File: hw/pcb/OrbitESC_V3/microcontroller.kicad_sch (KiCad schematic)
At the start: 57 parts, among them J1 USB_C_Receptacle_USB2.0, J11 CANH, J11 CANL, J11 GND, J13 Micro_SD_Card, SW1 Reset, SW2 DFU, U1 TLE9250X, U2 AT25SF128A-SHB-T, U3 STM32F446RETx, X1 ASE-24MHz

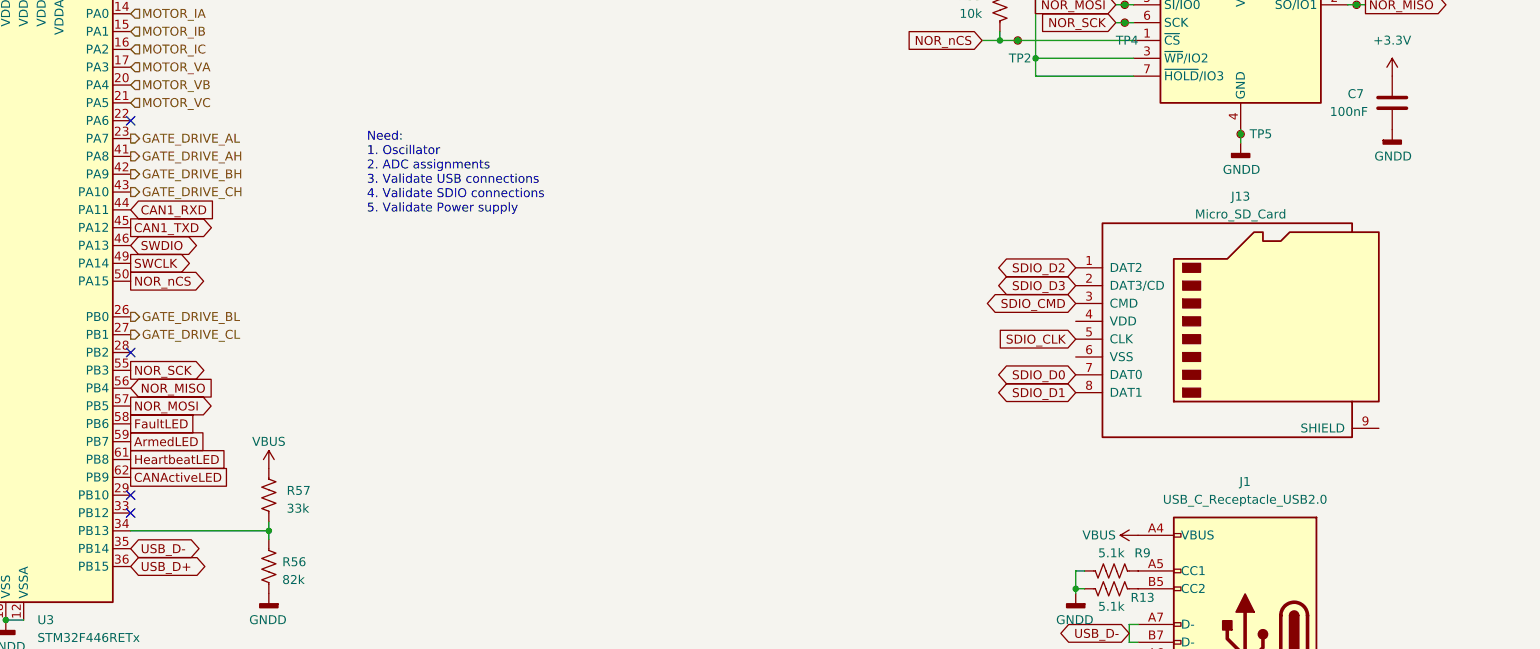
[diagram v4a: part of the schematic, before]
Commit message: Update SDIO card detect
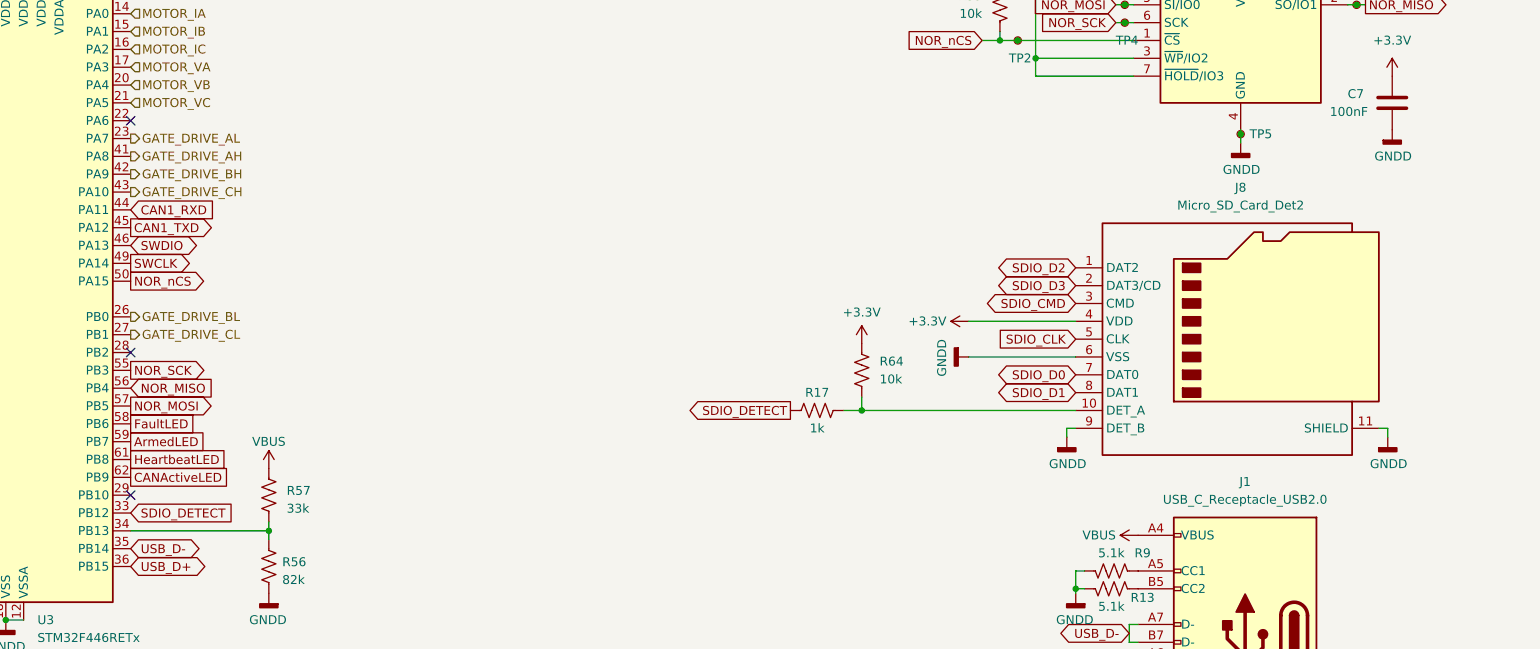
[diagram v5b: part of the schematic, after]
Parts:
- removed J13: Micro_SD_Card, symbol Connector:Micro_SD_Card
- added J8: Micro_SD_Card_Det2, symbol Connector:Micro_SD_Card_Det2
- added R17: 1k, Resistor_SMD:R_0402_1005Metric, symbol Device:R_US
- added R64: 10k, Resistor_SMD:R_0402_1005Metric, symbol Device:R_US
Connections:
- net +3.3V: now also J8.4 (VDD), R64.2
- net GND: now also J8.11 (SHIELD), J8.6 (VSS), J8.9 (DET_B)
- net SDIO_CLK: now also J8.5 (CLK)
- net SDIO_CMD: now also J8.3 (CMD)
- net SDIO_D0: now also J8.7 (DAT0)
- net SDIO_D1: now also J8.8 (DAT1)
- net SDIO_D2: now also J8.1 (DAT2)
- net SDIO_D3: now also J8.2 (DAT3/CD)
- net SDIO_DETECT: now reaches U3.33 (PB12)
- net SDIO_DETECT: now also R17.1
- new net: J8.10 (DET_A), R17.2, R64.1
- no-connect marks 17 -> 16
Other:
- note removed: "Need: 1. Oscillator 2. ADC assignments 3. Validate USB connections 4. Validate SDIO connections 5. Validate Power supply"

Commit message: Sync more work on schematic
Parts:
- C29: LCSC (none) -> C23733
- J8: footprint (none) -> Connector_Card:microSD_HC_Hirose_DM3D-SF; DigiKey (none) -> HR1941CT-ND
- R56: value 82k -> 100k; LCSC (none) -> C25741
- R57: value 33k -> 56k; LCSC (none) -> C25796
- U3: LCSC (none) -> C69336
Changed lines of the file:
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@@
       (effects (font (size 1.27 1.27)) hide)
     )
-    (property "LCSC" "" (at 145.415 205.74 0)
+    (property "LCSC" "C23733" (at 145.415 205.74 0)
       (effects (font (size 1.27 1.27)) hide)
     )
@@
     )
     (property "Datasheet" "https://www.st.com/resource/en/datasheet/stm32f446re.pdf" (at 177.8 175.26 0)
+      (effects (font (size 1.27 1.27)) hide)
+    )
+    (property "LCSC" "C69336" (at 177.8 175.26 0)
       (effects (font (size 1.27 1.27)) hide)
     )
@@
       (effects (font (size 1.27 1.27)) (justify left))
     )
-    (property "Value" "33k" (at 217.805 205.105 0)
+    (property "Value" "56k" (at 217.805 205.105 0)
       (effects (font (size 1.27 1.27)) (justify left))
     )
@@
       (effects (font (size 1.27 1.27)) hide)
     )
+    (property "LCSC" "C25796" (at 215.265 203.2 0)
+      (effects (font (size 1.27 1.27)) hide)
+    )
     (pin "1")
     (pin "2")
@@
       (effects (font (size 1.27 1.27)))
     )
-    (property "Footprint" "" (at 405.13 163.195 0)
+    (property "Footprint" "Connector_Card:microSD_HC_Hirose_DM3D-SF" (at 405.13 163.195 0)
       (effects (font (size 1.27 1.27)) hide)
     )
     (property "Datasheet" "https://www.hirose.com/en/product/document?clcode=&productname=&series=DM3&documenttype=Catalog&lang=en&documentid=D49662_en" (at 355.6 178.435 0)
+      (effects (font (size 1.27 1.27)) hide)
+    )
+    (property "DigiKey" "HR1941CT-ND" (at 353.06 180.975 0)
       (effects (font (size 1.27 1.27)) hide)
     )
@@
       (effects (font (size 1.27 1.27)) (justify left))
     )
-    (property "Value" "82k" (at 217.17 215.265 0)
+    (property "Value" "100k" (at 217.17 215.265 0)
       (effects (font (size 1.27 1.27)) (justify left))
     )
@@
       (effects (font (size 1.27 1.27)) hide)
     )
+    (property "LCSC" "C25741" (at 215.265 213.36 0)
+      (effects (font (size 1.27 1.27)) hide)
+    )

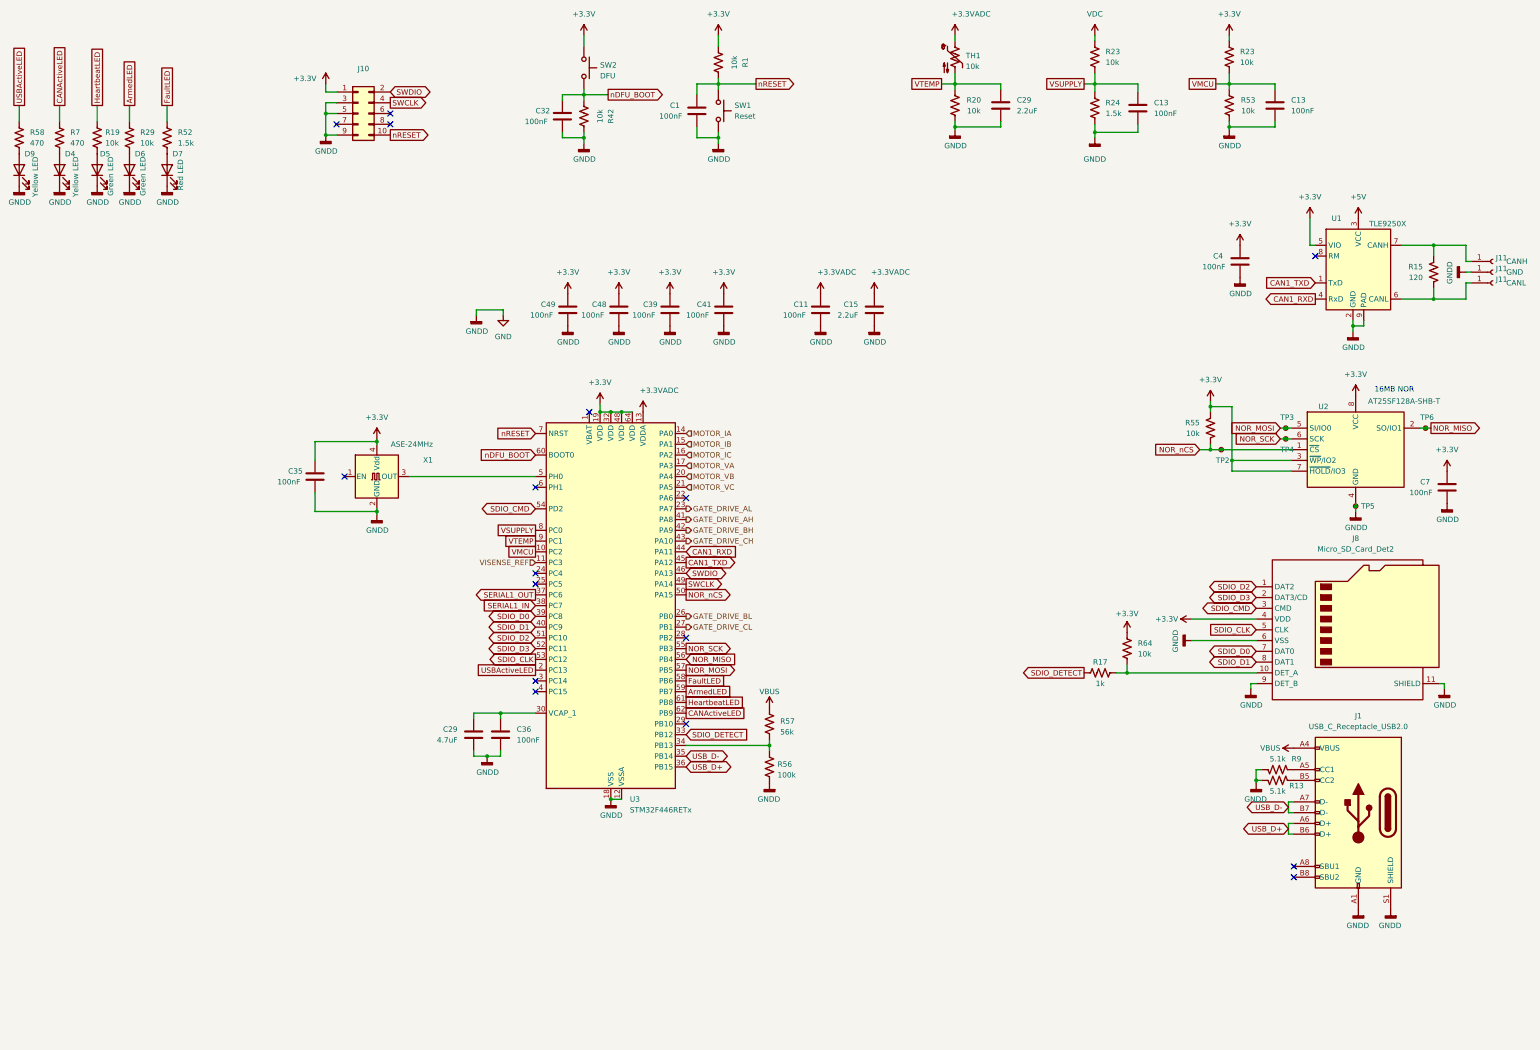
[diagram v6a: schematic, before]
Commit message: Semi-final schematic for F4 variant
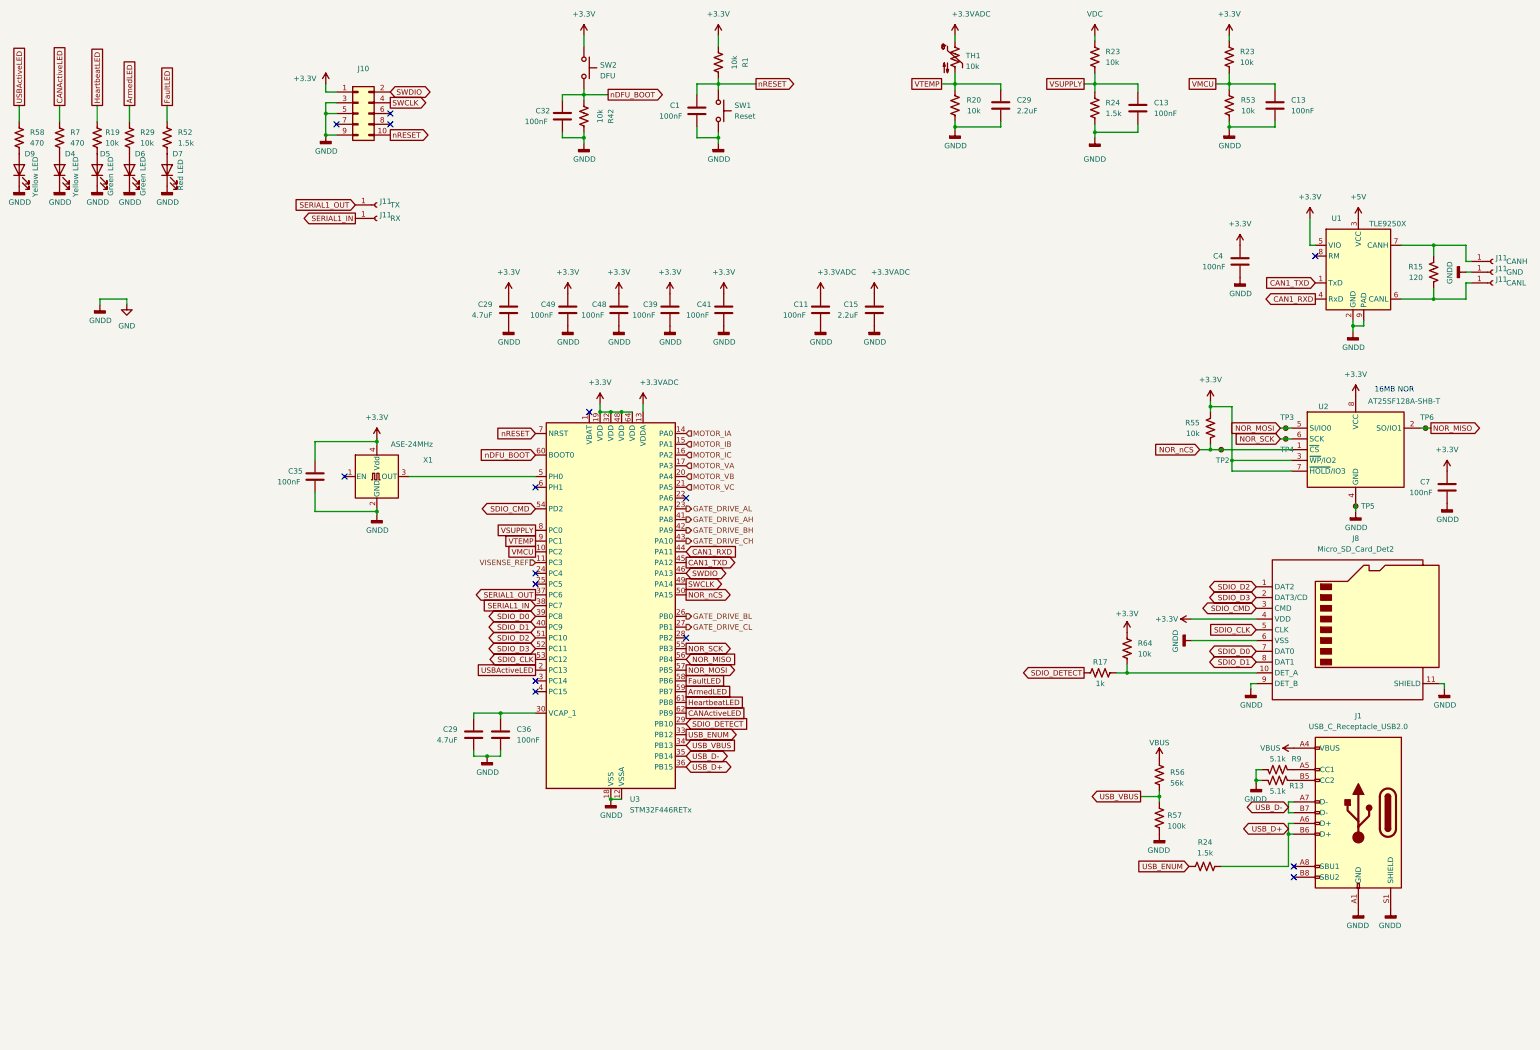
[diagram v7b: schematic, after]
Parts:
- added C29: 4.7uF, Capacitor_SMD:C_0402_1005Metric, symbol Device:C
- added J11: TX, TestPoint:TestPoint_Pad_1.5x1.5mm, symbol Connector:Conn_01x01_Female
- added J11: RX, TestPoint:TestPoint_Pad_1.5x1.5mm, symbol Connector:Conn_01x01_Female
- added R24: 1.5k, Resistor_SMD:R_0402_1005Metric, symbol Device:R_US
- J1: DigiKey (none) -> 2073-USB4085-GF-ACT-ND
- R56: value 100k -> 56k; LCSC C25741 -> C25796
- R57: value 56k -> 100k; LCSC C25796 -> C25741
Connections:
- net +3.3V: now also C29.2
- net GND: now also R57.2, C29.1; no longer R56.2
- net SDIO_DETECT: now also U3.29 (PB10); no longer U3.33 (PB12)
- net SERIAL1_IN: now also J11.1 (Pin_1)
- net SERIAL1_OUT: now also J11.1 (Pin_1)
- net USB_D+: now also R24.2
- net VBUS: now also R56.1; no longer R57.1
- new net USB_ENUM: R24.1, U3.33 (PB12)
- new net USB_VBUS: R56.2, R57.1, U3.34 (PB13)
- no-connect marks 16 -> 15

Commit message: Save tonight's PCB work
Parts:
- SW1, SW2: footprint Button_Switch_SMD:SW_SPST_PTS810 -> Button_Switch_SMD:SW_SPST_EVQP2; DigiKey CKN10502CT-ND -> P11081SCT-ND
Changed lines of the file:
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@@
       (effects (font (size 1.27 1.27)) (justify left))
     )
-    (property "Footprint" "Button_Switch_SMD:SW_SPST_PTS810" (at 176.53 48.26 0)
+    (property "Footprint" "Button_Switch_SMD:SW_SPST_EVQP2" (at 176.53 48.26 0)
       (effects (font (size 1.27 1.27)) hide)
     )
@@
       (effects (font (size 1.27 1.27)) hide)
     )
-    (property "DigiKey" "CKN10502CT-ND" (at 171.45 48.26 0)
+    (property "DigiKey" "P11081SCT-ND" (at 171.45 48.26 0)
       (effects (font (size 1.27 1.27)) hide)
     )
@@
       (effects (font (size 1.27 1.27)) (justify left))
     )
-    (property "Footprint" "Button_Switch_SMD:SW_SPST_PTS810" (at 208.28 58.42 0)
+    (property "Footprint" "Button_Switch_SMD:SW_SPST_EVQP2" (at 208.28 58.42 0)
       (effects (font (size 1.27 1.27)) hide)
     )
@@
       (effects (font (size 1.27 1.27)) hide)
     )
-    (property "DigiKey" "CKN10502CT-ND" (at 203.2 58.42 0)
-      (effects (font (size 1.27 1.27)) hide)
-    )
+    (property "DigiKey" "P11081SCT-ND" (at 203.2 58.42 0)
+      (effects (font (size 1.27 1.27)) hide)
+    )
